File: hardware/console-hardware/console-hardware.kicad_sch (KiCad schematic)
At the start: 7 parts

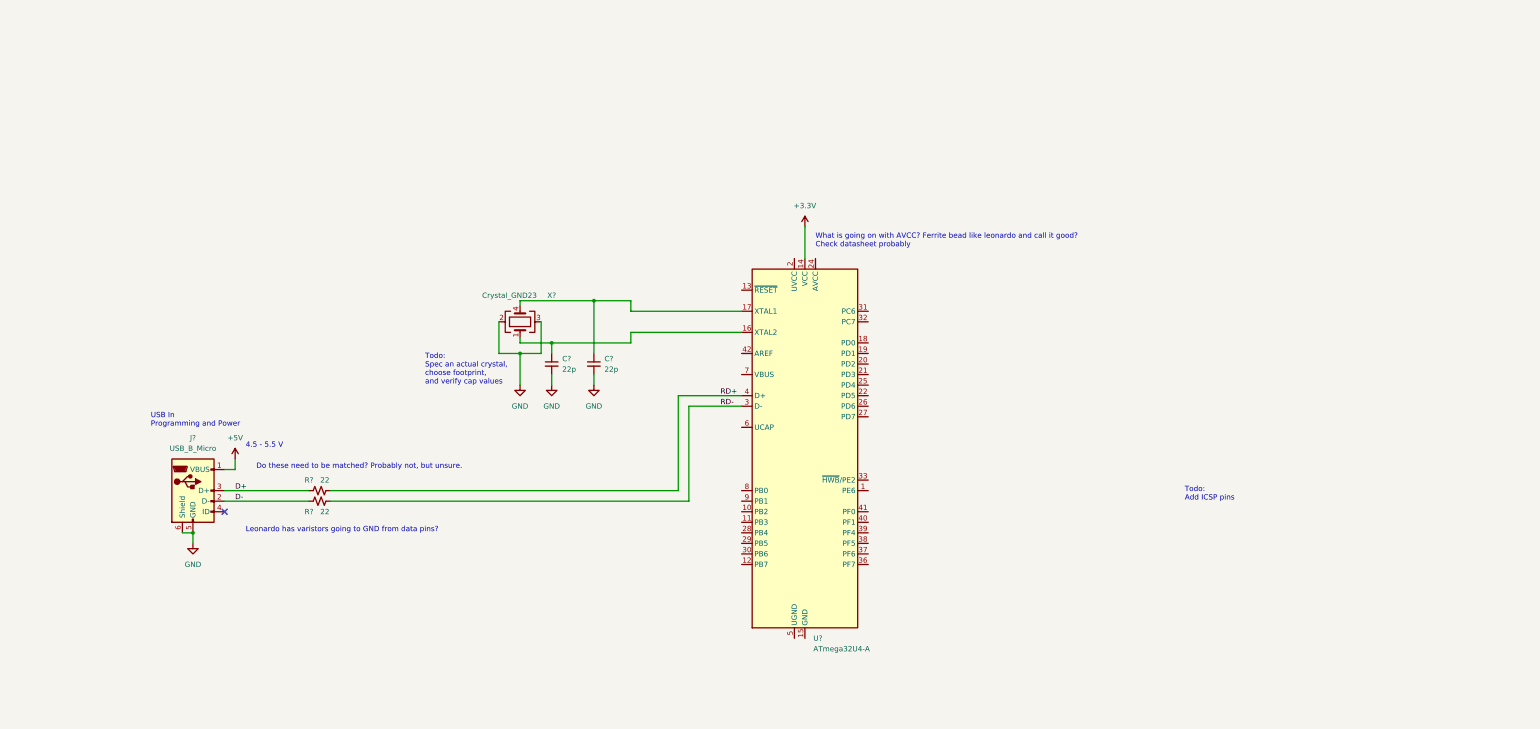
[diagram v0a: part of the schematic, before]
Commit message: Added 3.3v regulator and LiPo charger and more
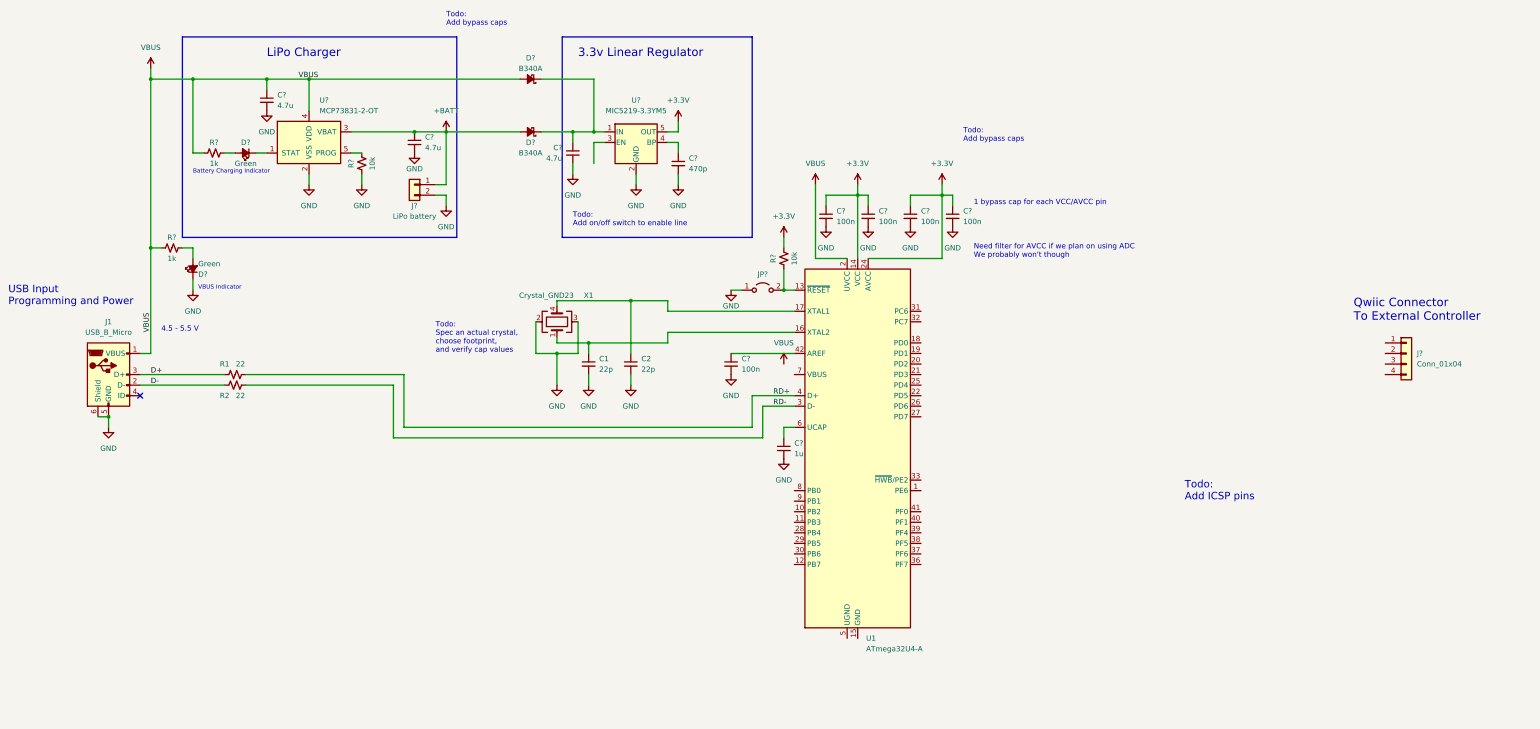
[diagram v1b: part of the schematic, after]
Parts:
- added C? (x5): 100n, symbol Device:C_Small
- added C? (x3): 4.7u, symbol Device:C_Small
- added C?: 470p, symbol Device:C_Small
- added C?: 1u, symbol Device:C_Small
- added D? (x2): Green, symbol Device:LED_Small_Filled
- added D? (x2): B340A, symbol Device:D_Schottky_Small_Filled
- added J?: Conn_01x04, symbol Connector_Generic:Conn_01x04
- added J?: LiPo battery, symbol Connector_Generic:Conn_01x02
- added JP?: Jumper_2_Open, symbol Jumper:Jumper_2_Open
- added R? (x2): 1k, symbol Device:R_Small_US
- added R? (x2): 10k, symbol Device:R_Small_US
- added U?: MIC5219-3.3YM5, Package_TO_SOT_SMD:SOT-23-5, symbol Regulator_Linear:MIC5219-3.3YM5
- added U?: MCP73831-2-OT, Package_TO_SOT_SMD:SOT-23-5, symbol U-MCP73831-2:MCP73831-2-OT
- gave numbers to parts that had none: 7
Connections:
- net +5V is gone; now on net VBUS: J1.1 (VBUS)
- net +3.3V: now also U1.24 (AVCC), U1.44 (AVCC), C?.1, C?.1, C?.1, C?.1, R?.2, U?.5 (OUT)
- net GND: now also C?.2, C?.2, C?.2, C?.2, C?.2, C?.2, C?.2, C?.2, C?.2, C?.2, D?.1 (K), J?.2 (Pin_2), JP?.1 (A), R?.1, U?.2 (GND), U?.2 (VSS)
- net at U1.13 (~{RESET}): now also JP?.2 (B), R?.1
- net VBUS: now reaches U1.2 (UVCC)
- net VBUS: now also C?.1, D?.2 (A), R?.1, R?.1, U?.4 (VDD)
- net at U1.42 (AREF): now also C?.1
- net at U1.6 (UCAP): now also C?.1
- new net: D?.1 (K), U?.1 (STAT)
- new net: D?.2 (A), R?.2 (x2)
- new net: C?.1, D?.1 (K), D?.1 (K), U?.1 (IN)
- new net: C?.1, U?.4 (BP)
- new net: R?.2, U?.5 (PROG)
- new net +BATT: C?.1, D?.2 (A), J?.1 (Pin_1), U?.3 (VBAT)
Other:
- note added: "1 bypass cap for each VCC/AVCC pin"
- note added: "3.3v Linear Regulator"
- note added: "Battery Charging Indicator"
- note added: "LiPo Charger"
- note added: "Need filter for AVCC if we plan on using ADC We probably won't though"
- note added: "Qwiic Connector To External Controller"
- note added: "Todo: Add bypass caps"
- note added: "Todo: Add on/off switch to enable line"
- note added: "USB Input Programming and Power"
- note added: "VBUS Indicator"
- note removed: "Do these need to be matched? Probably not, but unsure."
- note removed: "Leonardo has varistors going to GND from data pins?"
- note removed: "USB In Programming and Power"
- note removed: "What is going on with AVCC? Ferrite bead like leonardo and call it good? Check datasheet probably"
- moved on the sheet: C1, C2, J1, R1, R2, U1, X1

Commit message: Added buttons and display to schematic, plus some other changes
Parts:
- added J4: Conn_01x04, symbol Connector_Generic:Conn_01x04
- added R10, R11: 0, symbol Device:R_Small_US
- added R7: 10k, symbol Device:R_Small_US
- added R8, R9: 4.7k, symbol Device:R_Small_US
- added SW1, SW2, SW3, SW4, SW5, SW6: SW_Push, symbol Switch:SW_Push
- gave numbers to parts that had none: 23
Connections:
- net +3.3V: now also J3.2 (Pin_2), J4.2 (Pin_2), R8.2, R9.2
- net GND: now also J3.1 (Pin_1), U1.15 (GND), U1.23 (GND), U1.35 (GND), U1.43 (GND), U1.5 (UGND), J4.1 (Pin_1), R7.1, SW1.2, SW2.2, SW3.2, SW4.2, SW5.2, SW6.2
- net VBUS: now also U1.7 (VBUS)
- net SCL: now reaches U1.18 (PD0)
- net SCL: now also R10.2, R8.1
- net SDA: now reaches U1.19 (PD1)
- net SDA: now also R11.1, R9.1
- net at U1.33 (~{HWB}/PE2): now also R7.2
- net at U1.36 (PF7): now also SW6.1
- net at U1.37 (PF6): now also SW5.1
- net at U1.38 (PF5): now also SW4.1
- net at U1.39 (PF4): now also SW3.1
- net at U1.40 (PF1): now also SW2.1
- net at U1.41 (PF0): now also SW1.1
- net at J3.3 (Pin_3): now also J4.3 (Pin_3), R11.2
- net at J3.4 (Pin_4): now also J4.4 (Pin_4), R10.1
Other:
- note added: "Add pullups?"
- note added: "Qwiic Connector To Display"
- note added: "Todo: Spec Buttons"
- note added: "Todo: Spec final display"
- note added: "User Input Buttons"
- note added: "Verify I2C pullup values"
- note removed: "ATMEGA32U4 design based on Arduino Leonardo schematic"

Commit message: Updated schematic and added preliminary layout
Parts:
- removed J4: Conn_01x04, symbol Connector_Generic:Conn_01x04
- added J4: ICSP, Connector_PinHeader_2.54mm:PinHeader_2x03_P2.54mm_Vertical, symbol Connector_Generic:Conn_02x03_Odd_Even
- added J5: Conn_01x20, Connector_PinHeader_2.54mm:PinHeader_1x20_P2.54mm_Vertical, symbol Connector_Generic:Conn_01x20
- C1, C2: value 22p -> 30p
- C10, C11, C12, C3, C4, C5, C6, C7, C8, C9: footprint (none) -> Capacitor_SMD:C_0805_2012Metric
- D1, D2: footprint (none) -> LED_SMD:LED_0805_2012Metric
- D3, D4: footprint (none) -> Diode_SMD:D_SMA
- J1: footprint (none) -> Connector_USB:USB_Micro-B_Amphenol_10104110_Horizontal
- J2: footprint (none) -> Connector_JST:JST_PH_S2B-PH-K_1x02_P2.00mm_Horizontal
- J3: footprint (none) -> Connector_JST:JST_SH_SM04B-SRSS-TB_1x04-1MP_P1.00mm_Horizontal
- R1, R10, R11, R2, R3, R4, R5, R6, R7, R8, R9: footprint (none) -> Resistor_SMD:R_0805_2012Metric
- SW1, SW2, SW3, SW4, SW5, SW6: footprint (none) -> Button_Switch_SMD:SW_SPST_TL3305A
- X1: value Crystal_GND23 -> 16 MHz; footprint (none) -> Crystal:Crystal_SMD_2520-4Pin_2.5x2.0mm
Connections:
- net +3.3V: now also J4.2 (Pin_2), J5.3 (Pin_3)
- net GND: now also J4.6 (Pin_6), J5.4 (Pin_4)
- net MOSI: now reaches U1.10 (PB2)
- net MOSI: now also J4.4 (Pin_4)
- net MISO: now reaches U1.11 (PB3)
- net MISO: now also J4.1 (Pin_1)
- net ~{RESET}: now reaches JP1.2 (B), R6.1, U1.13 (~{RESET})
- net ~{RESET}: now also J4.5 (Pin_5)
- net SCK: now reaches U1.9 (PB1)
- net SCK: now also J4.3 (Pin_3)
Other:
- note added: "Display Module"
- note added: "ICSP"
- note added: "Update Connections"
- note removed: "Need filter for AVCC if we plan on using ADC We probably won't though"
- note removed: "Qwiic Connector To Display"
- note removed: "Todo: Add ICSP pins"
- note removed: "Todo: Add bypass caps"
- note removed: "Todo: Spec an actual crystal, choose footprint, and verify cap values"
- note removed: "Todo: Spec final display"
- moved on the sheet: C1, C10, C11, C12, C2, C3, C4, C5, C6, C7, C8, C9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

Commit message: Updated schematic and layout. Added BOM
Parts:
- added D5: Green, LED_SMD:LED_0805_2012Metric, symbol Device:LED_Small_Filled
- added R12: 4.7k, Resistor_SMD:R_0805_2012Metric, symbol Device:R_Small_US
- added R13, R14, R15, R16, R17, R18: 10k, Resistor_SMD:R_0805_2012Metric, symbol Device:R_Small_US
- added SW7: SW_SPDT, Button_Switch_THT:SW_E-Switch_EG1224_SPDT_Angled, symbol Switch:SW_SPDT
- C1, C2: DIS (none) -> Digi-Key; DPN (none) -> 738-CML0805C0G300JT50VCT-ND; MFR (none) -> Stackpole; MPN (none) -> CML0805C0G300JT50V
- C10, C11, C12, C7, C9: DIS (none) -> Digi-Key; DPN (none) -> 1276-1099-1-ND; MFR (none) -> Samsung; MPN (none) -> CL21B104KACNNNC
- C3, C4, C5: DIS (none) -> Digi-Key; DPN (none) -> 1276-6462-1-ND; MFR (none) -> Samsung; MPN (none) -> CL21A475KAQNNNG
- C6: DIS (none) -> Digi-Key; DPN (none) -> 1276-2515-1-ND; MFR (none) -> Samsung; MPN (none) -> CL21B471KBANFNC
- C8: DIS (none) -> Digi-Key; DPN (none) -> 1276-1066-1-ND; MFR (none) -> Samsung; MPN (none) -> CL21B105KAFNNNE
- D1, D2: DIS (none) -> Digi-Key; DPN (none) -> 511-1287-1-ND; MFR (none) -> Rohm; MPN (none) -> SML-210MTT86
- D3, D4: DIS (none) -> Digi-Key; DPN (none) -> B340A-M3/61TGICT-ND; MFR (none) -> Vishay; MPN (none) -> B340A-M3/61T
- J1: DIS (none) -> Digi-Key; DPN (none) -> WM1398CT-ND; MFR (none) -> Molex; MPN (none) -> 0476420001
- J2: DIS (none) -> Digi-Key; DPN (none) -> 455-1719-ND; MFR (none) -> JST; MPN (none) -> S2B-PH-K-S(LF)(SN)
- J3: DIS (none) -> Adafruit; DPN (none) -> 4208
- J4: DIS (none) -> Digi-Key; DPN (none) -> 952-2121-ND; MFR (none) -> Harwin; MPN (none) -> M20-9980346
- J5: DIS (none) -> Adafruit
- JP1: footprint (none) -> Jumper:SolderJumper-2_P1.3mm_Open_Pad1.0x1.5mm
- R1, R2: DIS (none) -> Digi-Key; DPN (none) -> 13-RC0805FR-1322RLCT-ND; MFR (none) -> Yageo; MPN (none) -> RC0805FR-1322RL
- R10, R11: DIS (none) -> Digi-Key; DPN (none) -> 311-0.0ARCT-ND; MFR (none) -> Yageo; MPN (none) -> RC0805JR-070RL
- R3, R4: value 1k -> 4.7k; DIS (none) -> Digi-Key; DPN (none) -> 311-4.7KARCT-ND; MFR (none) -> Yageo; MPN (none) -> RC0805JR-074K7L
- R5, R6, R7: DIS (none) -> Digi-Key; DPN (none) -> 311-10KARCT-ND; MFR (none) -> Yageo; MPN (none) -> RC0805JR-0710KL
- R8, R9: DIS (none) -> Digi-Key; DPN (none) -> 311-4.7KARCT-ND; MFR (none) -> Yageo; MPN (none) -> RC0805JR-074K7L
- SW1, SW2, SW3, SW4, SW5, SW6: DIS (none) -> Adafruit; DPN (none) -> 1010
- U1: DIS (none) -> Digi-Key; DPN (none) -> ATMEGA32U4-AU-ND; MFR (none) -> Microchip; MPN (none) -> ATMEGA32U4-AU
- U2: DIS (none) -> Digi-Key; DPN (none) -> MCP73831T-2DCI/OTCT-ND; MFR (none) -> Microchip; MPN (none) -> MCP73831T-2DCI/OT
- U3: DIS (none) -> Digi-Key; DPN (none) -> 576-1281-1-ND; MFR (none) -> Microchip; MPN (none) -> MIC5219-3.3YM5-TR
- X1: DIS (none) -> Digi-Key; DPN (none) -> 1923-830011263CT-ND; MFR (none) -> Wurth; MPN (none) -> 830011263
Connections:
- net +3.3V: now also J5.1 (Pin_1), R12.1, R13.1, R14.1, R15.1, R16.1, R17.1, R18.1; no longer J5.3 (Pin_3)
- net GND: now also J5.11 (Pin_11), J5.2 (Pin_2), D5.1 (K), SW7.1 (A); no longer J5.4 (Pin_4)
- net MISO: now also J5.5 (Pin_5)
- net MOSI: now also J5.6 (Pin_6)
- net SCK: now also J5.4 (Pin_4)
- net SCL: now also J5.14 (Pin_14)
- net SDA: now also J5.13 (Pin_13)
- net at SW5.1, U1.37 (PF6): now also R17.2
- net at C5.1, D3.1 (K), D4.1 (K)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: now also SW7.3 (C)
- net at SW3.1, U1.39 (PF4): now also R15.2
- net DISPLAY_IRQ: now reaches U1.12 (PB7)
- net DISPLAY_IRQ: now also J5.12 (Pin_12)
- net DISPLAY_CS: now reaches U1.27 (PD7)
- net DISPLAY_CS: now also J5.7 (Pin_7)
- net DISPLAY_DC: now reaches U1.28 (PB4)
- net DISPLAY_DC: now also J5.8 (Pin_8)
- net DISPLAY_RST: now reaches U1.29 (PB5)
- net DISPLAY_RST: now also J5.9 (Pin_9)
- net DISPLAY_LITE: now reaches U1.30 (PB6)
- net DISPLAY_LITE: now also J5.10 (Pin_10)
- net at SW6.1, U1.36 (PF7): now also R18.2
- net at SW4.1, U1.38 (PF5): now also R16.2
- net at SW2.1, U1.40 (PF1): now also R14.2
- net at SW1.1, U1.41 (PF0): now also R13.2
- net SDA_OUT: now reaches J3.3 (Pin_3), R11.2
- net SCL_OUT: now reaches J3.4 (Pin_4), R10.1
- net ON/~{OFF}: now reaches U3.3 (EN)
- net ON/~{OFF}: now also SW7.2 (B)
- new net: D5.2 (A), R12.2
- new net 3VO: J5.3 (Pin_3)
- no-connect marks 1 -> 17
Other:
- note added: "Adafruit TFT LCD w/ Capacitive Touch"
- note added: "On/off Indicator"
- note added: "PWM Brightness Control"
- note removed: "Add pullups?"
- note removed: "Todo: Add on/off switch to enable line"
- note removed: "Update Connections"
- moved on the sheet: D3, D4, J4, J5, R10, R11, SW1, SW2, SW3, SW4, SW5, SW6
